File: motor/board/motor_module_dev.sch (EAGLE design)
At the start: 96 parts, among them IC6 LTC6088, IC7 DRV8833RTY

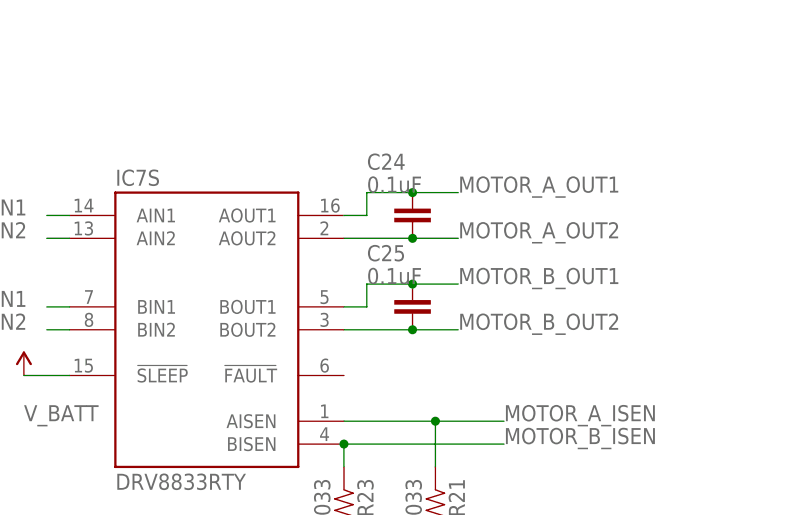
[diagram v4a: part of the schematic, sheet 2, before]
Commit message: Prepared silkscreen
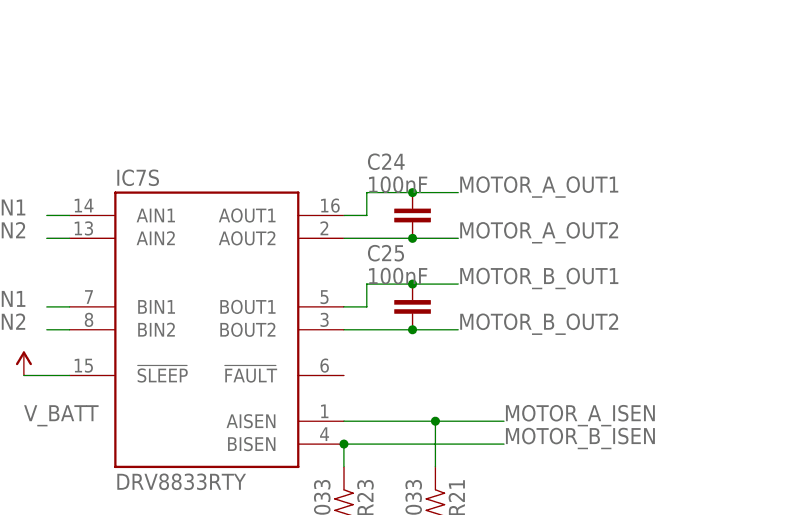
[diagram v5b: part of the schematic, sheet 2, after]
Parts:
- C1, C30, C7, C8: VOLTAGE (none) -> 10V
- C10, C11, C2, C29, C3, C4, C41, C43, C44, C5, C6, C9: VOLTAGE (none) -> 6.3V
- C24, C25: value 0.1uF -> 100nF

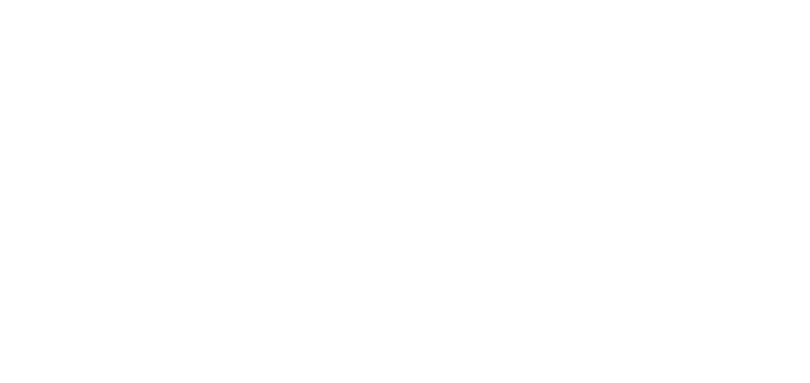
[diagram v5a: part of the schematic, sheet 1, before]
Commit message: Fixing small things preparing for panelization
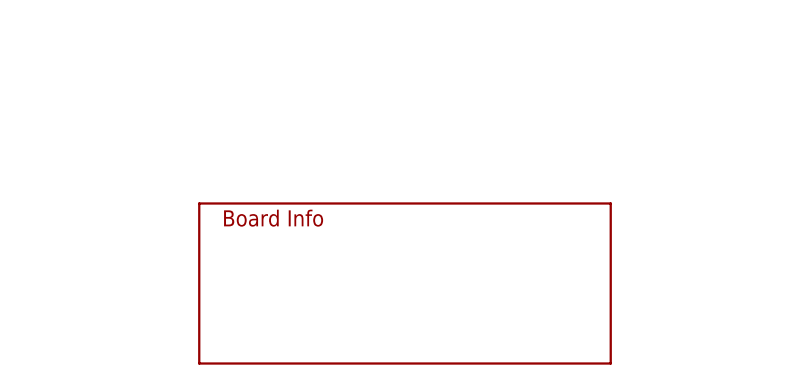
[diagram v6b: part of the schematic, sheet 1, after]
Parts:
- added U$31: INFO, modular_robotics:INFO
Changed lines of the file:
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@@
 <part name="R41" library="biomimetic" deviceset="RESISTOR" device="0402-RES" value="470R"/>
 <part name="R42" library="biomimetic" deviceset="RESISTOR" device="0402-RES" value="480R"/>
+<part name="U$31" library="modular_robotics" deviceset="INFO" device="">
+<attribute name="AUTHOR" value="Austin Buchan"/>
+<attribute name="DATE" value="Feb. 2014"/>
+<attribute name="DESIGN" value="Motor Control Dev"/>
+<attribute name="ORGANIZATION" value="UC Berkeley Biomimetic Millisystems Lab"/>
+<attribute name="REVISION" value="r0.0"/>
+</part>
 </parts>
 <sheets>
@@
 </instance>
 <instance part="GND14" gate="1" x="101.6" y="101.6" rot="R270"/>
+<instance part="U$31" gate="G$1" x="101.6" y="5.08">
+<attribute name="AUTHOR" x="101.6" y="5.08" size="1.778" layer="96" display="off"/>
+<attribute name="DATE" x="101.6" y="5.08" size="1.778" layer="96" display="off"/>
+<attribute name="DESIGN" x="101.6" y="5.08" size="1.778" layer="96" display="off"/>
+<attribute name="ORGANIZATION" x="101.6" y="5.08" size="1.778" layer="96" display="off"/>
+<attribute name="REVISION" x="101.6" y="5.08" size="1.778" layer="96" display="off"/>
+</instance>
 </instances>
 <busses>

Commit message: Board and component orders placed
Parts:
- C42: VOLTAGE (none) -> 6.3V
- R2: value 5k -> 5k1
- R42: value 480R -> 470R
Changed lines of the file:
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@@
 <part name="U$11" library="modular_robotics" deviceset="INA199A1" device=""/>
 <part name="R1" library="biomimetic" deviceset="RESISTOR" device="0603-RES" value="0R033"/>
-<part name="R2" library="biomimetic" deviceset="RESISTOR" device="0402-RES" value="5k"/>
+<part name="R2" library="biomimetic" deviceset="RESISTOR" device="0402-RES" value="5k1"/>
 <part name="R3" library="biomimetic" deviceset="RESISTOR" device="0402-RES" value="10k"/>
 <part name="R4" library="biomimetic" deviceset="RESISTOR" device="0402-RES" value="20k"/>
@@
 </part>
 <part name="R30" library="biomimetic" deviceset="RESISTOR" device="0402-RES" value="1k"/>
-<part name="C42" library="biomimetic" deviceset="CAP" device="0402-CAP" value="2.2nF"/>
+<part name="C42" library="biomimetic" deviceset="CAP" device="0402-CAP" value="2.2nF">
+<attribute name="VOLTAGE" value="6.3V"/>
+</part>
 <part name="R31" library="biomimetic" deviceset="RESISTOR" device="0402-RES" value="1k"/>
 <part name="C43" library="biomimetic" deviceset="CAP" device="0402-CAP" value="2.2nF">
@@
 <part name="R40" library="biomimetic" deviceset="RESISTOR" device="0402-RES" value="470R"/>
 <part name="R41" library="biomimetic" deviceset="RESISTOR" device="0402-RES" value="470R"/>
-<part name="R42" library="biomimetic" deviceset="RESISTOR" device="0402-RES" value="480R"/>
+<part name="R42" library="biomimetic" deviceset="RESISTOR" device="0402-RES" value="470R"/>
 <part name="U$31" library="modular_robotics" deviceset="INFO" device="">
 <attribute name="AUTHOR" value="Austin Buchan"/>
@@
 </instance>
 <instance part="R30" gate="G$1" x="172.72" y="167.64"/>
-<instance part="C42" gate="G$1" x="180.34" y="127"/>
+<instance part="C42" gate="G$1" x="180.34" y="127">
+<attribute name="VOLTAGE" x="180.34" y="127" size="1.778" layer="96" display="off"/>
+</instance>
 <instance part="R31" gate="G$1" x="172.72" y="132.08"/>
 <instance part="C43" gate="G$1" x="180.34" y="88.9">

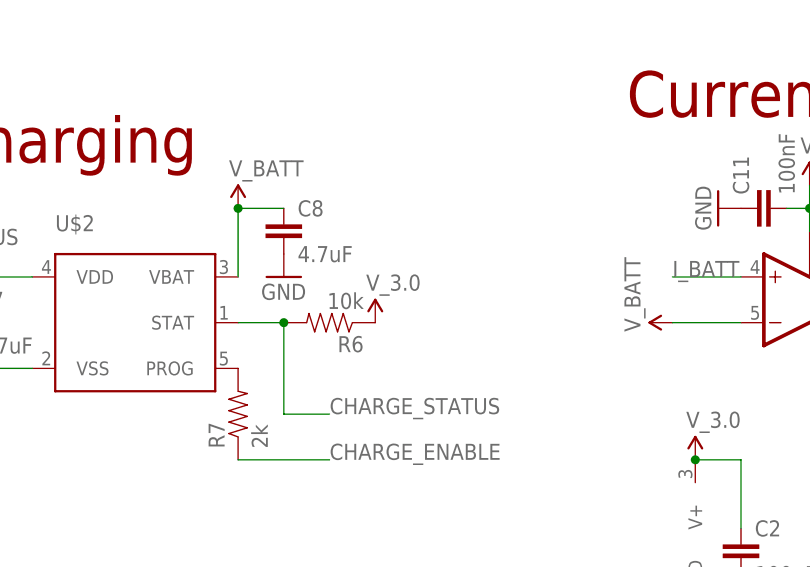
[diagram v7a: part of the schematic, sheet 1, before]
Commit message: Moved pullup on charge management status to vbus
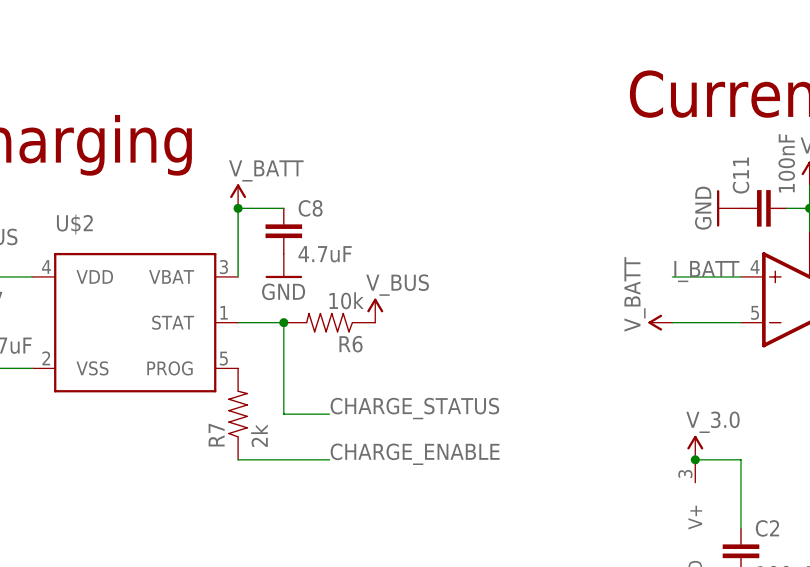
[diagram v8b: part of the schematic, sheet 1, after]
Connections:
- net V_3.0: no longer R6.1
- net V_BUS: now also R6.1
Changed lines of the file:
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@@
 <part name="U$6" library="modular_robotics" deviceset="V_BUS" device=""/>
 <part name="U$7" library="modular_robotics" deviceset="V_BUS" device=""/>
-<part name="U$9" library="modular_robotics" deviceset="V_3.0" device=""/>
 <part name="U$10" library="modular_robotics" deviceset="V_3.0" device=""/>
 <part name="U$12" library="modular_robotics" deviceset="V_3.0" device=""/>
@@
 <attribute name="REVISION" value="r0.0"/>
 </part>
+<part name="U$9" library="modular_robotics" deviceset="V_BUS" device=""/>
 </parts>
 <sheets>
@@
 <instance part="U$6" gate="G$1" x="17.78" y="93.98"/>
 <instance part="U$7" gate="G$1" x="177.8" y="104.14"/>
-<instance part="U$9" gate="G$1" x="63.5" y="88.9"/>
 <instance part="U$10" gate="G$1" x="99.06" y="73.66"/>
 <instance part="U$12" gate="G$1" x="213.36" y="104.14"/>
@@
 <attribute name="REVISION" x="101.6" y="5.08" size="1.778" layer="96" display="off"/>
 </instance>
+<instance part="U$9" gate="G$1" x="63.5" y="88.9"/>
 </instances>
 <busses>
@@
 <wire x1="190.5" y1="58.42" x2="190.5" y2="55.88" width="0.1524" layer="91"/>
 </segment>
+<segment>
+<pinref part="R6" gate="G$1" pin="1"/>
+<pinref part="U$9" gate="G$1" pin="V_BUS"/>
+</segment>
 </net>
 <net name="N$4" class="0">
@@
 <net name="V_3.0" class="0">
 <segment>
-<pinref part="R6" gate="G$1" pin="1"/>
-<pinref part="U$9" gate="G$1" pin="V_3.0"/>
-</segment>
-<segment>
 <pinref part="C2" gate="G$1" pin="1"/>
